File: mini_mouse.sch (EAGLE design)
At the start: 33 parts, among them IC1 PIC18F4550_TQFP, IC2 L298, IC3 LP2950CDT-5.0

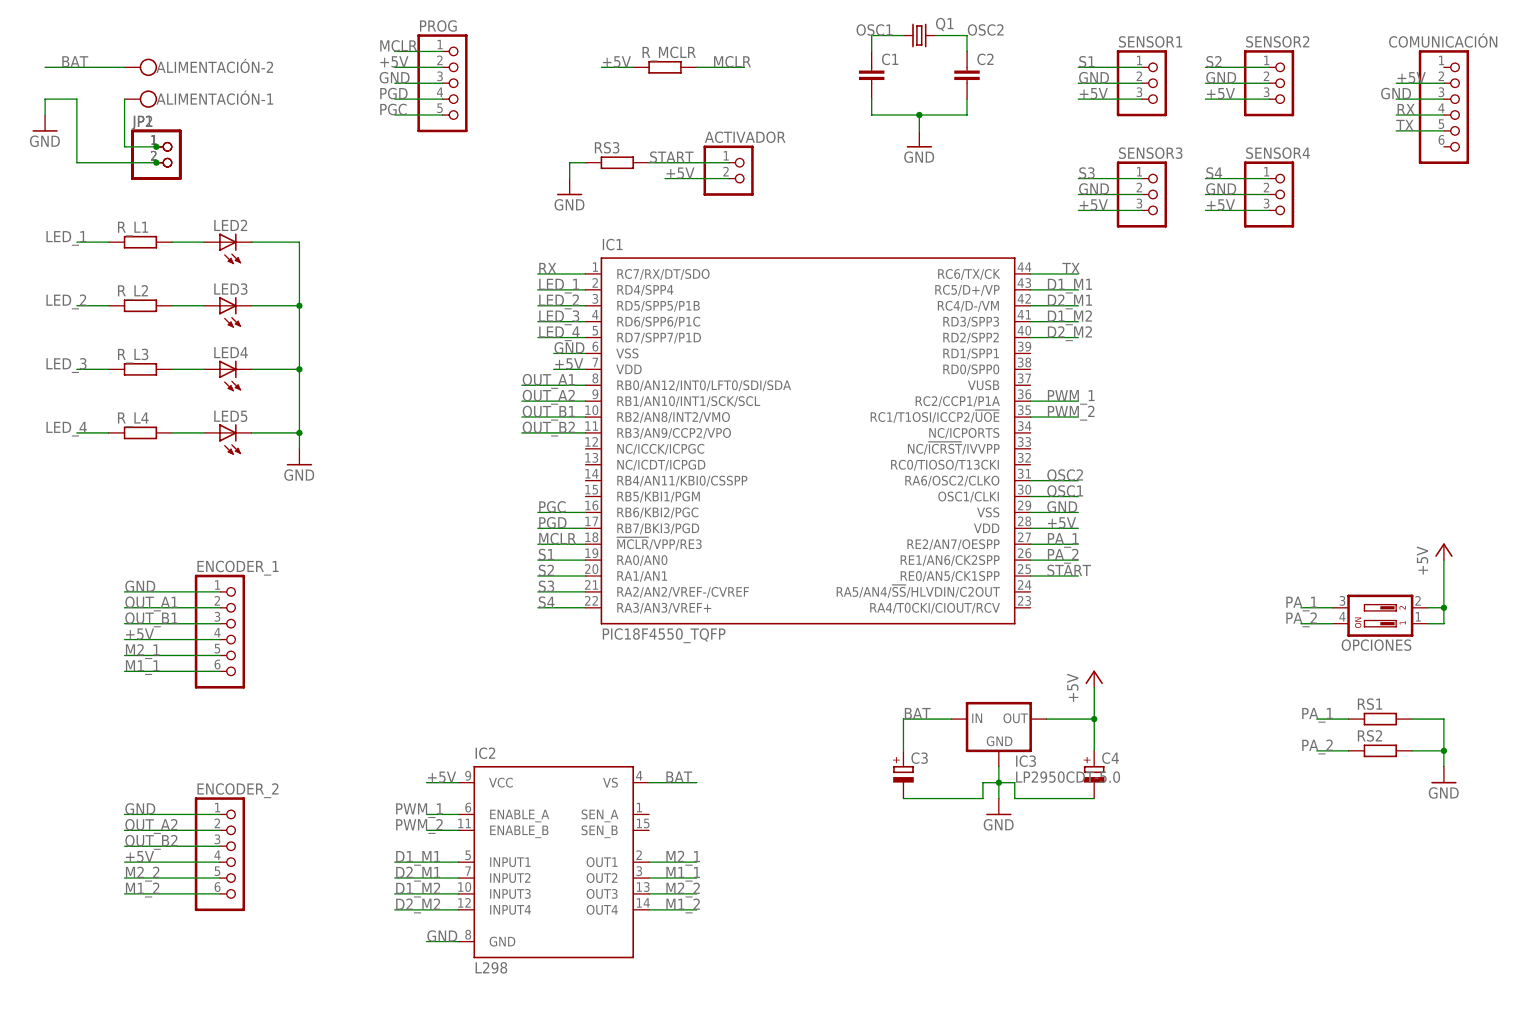
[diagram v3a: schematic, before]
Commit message: Cambios finales a esquemático, inicio de board
Se realizaron los ultimos cambios al esquemático. Se empezó el diseño del pcb
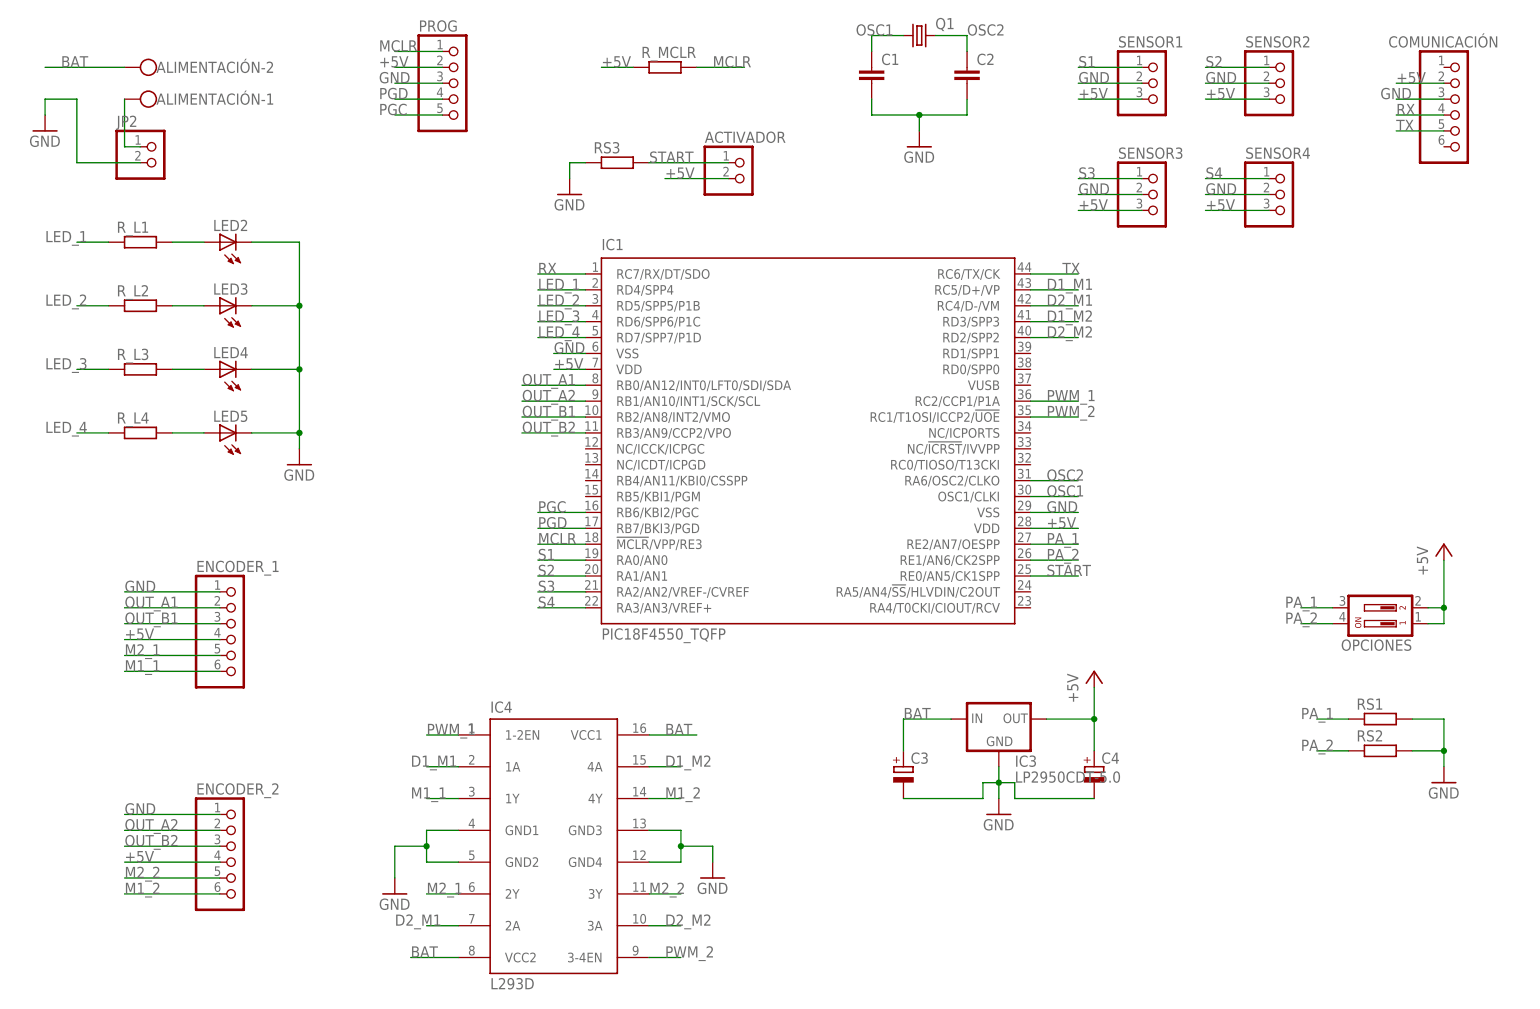
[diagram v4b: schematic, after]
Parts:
- removed IC2: L298, st-microelectronics:L298
- removed JP1: (no value), pinhead:PINHD-1X2
- added IC4: L293D, st-microelectronics:L293D
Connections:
- net +5V: no longer IC2.VCC
- net BAT: now also IC4.VCC1, IC4.VCC2; no longer IC2.VS
- net D1_M1: now also IC4.1A; no longer IC2.INPUT1
- net D1_M2: now also IC4.4A; no longer IC2.INPUT3
- net D2_M1: now also IC4.2A; no longer IC2.INPUT2
- net D2_M2: now also IC4.3A; no longer IC2.INPUT4
- net GND: now also IC4.GND1, IC4.GND2, IC4.GND3, IC4.GND4; no longer IC2.GND, JP1.2
- net M1_1: now also IC4.1Y; no longer IC2.OUT2
- net M1_2: now also IC4.4Y; no longer IC2.OUT4
- net M2_1: now also IC4.2Y; no longer IC2.OUT1
- net M2_2: now also IC4.3Y; no longer IC2.OUT3
- net N$5: no longer JP1.1
- net PWM_1: now also IC4.1-2EN; no longer IC2.ENABLE_A
- net PWM_2: now also IC4.3-4EN; no longer IC2.ENABLE_B
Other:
- moved on the sheet: JP2

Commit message: pcb
Se realizò PCB en un 90%
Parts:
- C3, C4: device rcl:CPOL-EU153CLV-0405 -> rcl:CPOL-EUE5-6
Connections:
- net D1_M1: now also IC1.RA4/T0CKI/CIOUT/RCV; no longer IC1.RC5/D+/VP
- net D1_M2: now also IC1.RB5/KBI1/PGM; no longer IC1.RD3/SPP3
- net D2_M1: now also IC1.RA5/AN4/!SS!/HLVDIN/C2OUT; no longer IC1.RC4/D-/VM
- net D2_M2: now also IC1.RB4/AN11/KBI0/CSSPP; no longer IC1.RD2/SPP2
- net LED_1: now also IC1.RC5/D+/VP
- net LED_2: now also IC1.RC4/D-/VM
- net LED_3: now also IC1.RD3/SPP3
- net LED_4: now also IC1.RD2/SPP2
- net M1_2: now also IC4.3Y; no longer IC4.4Y
- net M2_2: now also IC4.4Y; no longer IC4.3Y
- net OUT_B1: now also IC1.RB3/AN9/CCP2/VPO; no longer IC1.RB2/AN8/INT2/VMO
- net OUT_B2: now also IC1.RB2/AN8/INT2/VMO; no longer IC1.RB3/AN9/CCP2/VPO
- net PWM_1: now also IC1.RC1/T1OSI/ICCP2/!UOE; no longer IC1.RC2/CCP1/P1A
- net PWM_2: now also IC1.RC2/CCP1/P1A; no longer IC1.RC1/T1OSI/ICCP2/!UOE

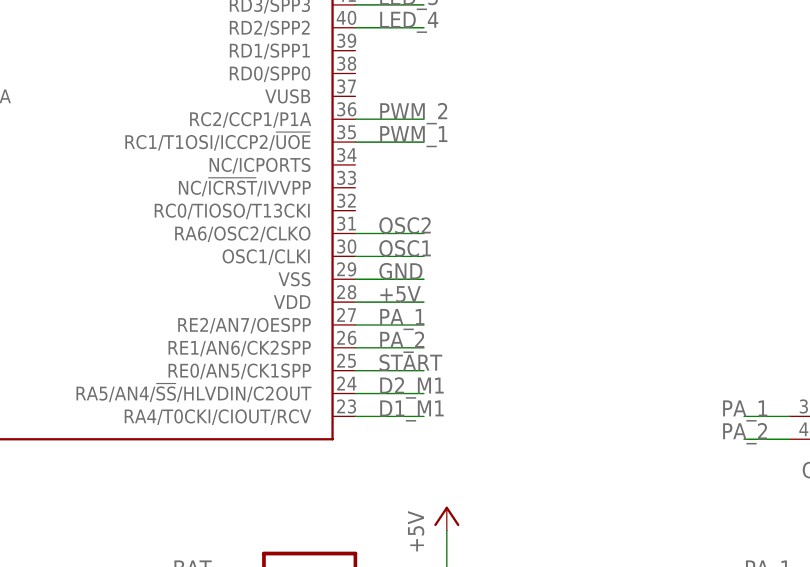
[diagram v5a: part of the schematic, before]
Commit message: Pads correctos
Se agregaron los pads deseados y se terminaron de cablear componentes faltantes
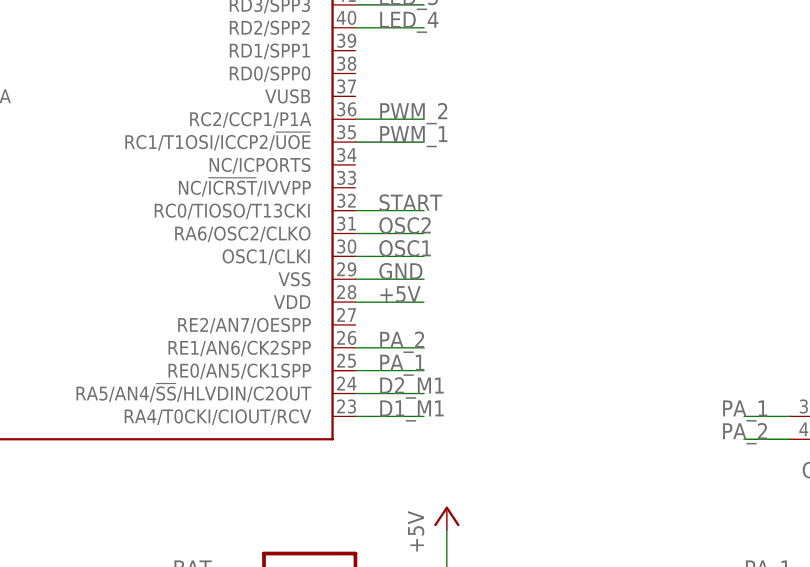
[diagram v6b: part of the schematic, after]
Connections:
- net PA_1: now also IC1.RE0/AN5/CK1SPP; no longer IC1.RE2/AN7/OESPP
- net START: now also IC1.RC0/TIOSO/T13CKI; no longer IC1.RE0/AN5/CK1SPP
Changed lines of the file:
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@@
 <net name="PA_1" class="0">
-<segment>
-<pinref part="IC1" gate="G$1" pin="RE2/AN7/OESPP"/>
-<wire x1="170.18" y1="83.82" x2="177.8" y2="83.82" width="0.1524" layer="91"/>
-<label x="172.72" y="83.82" size="1.778" layer="95"/>
-</segment>
 <segment>
 <pinref part="OPCIONES" gate="1" pin="3"/>
@@
 <label x="213.36" y="55.88" size="1.778" layer="95"/>
 </segment>
+<segment>
+<pinref part="IC1" gate="G$1" pin="RE0/AN5/CK1SPP"/>
+<wire x1="170.18" y1="78.74" x2="177.8" y2="78.74" width="0.1524" layer="91"/>
+<label x="172.72" y="78.74" size="1.778" layer="95"/>
+</segment>
 </net>
 <net name="PA_2" class="0">
-<segment>
-<pinref part="IC1" gate="G$1" pin="RE1/AN6/CK2SPP"/>
-<wire x1="170.18" y1="81.28" x2="177.8" y2="81.28" width="0.1524" layer="91"/>
-<label x="172.72" y="81.28" size="1.778" layer="95"/>
-</segment>
 <segment>
 <pinref part="OPCIONES" gate="1" pin="4"/>
@@
 <wire x1="220.98" y1="50.8" x2="215.9" y2="50.8" width="0.1524" layer="91"/>
 <label x="213.36" y="50.8" size="1.778" layer="95"/>
+</segment>
+<segment>
+<pinref part="IC1" gate="G$1" pin="RE1/AN6/CK2SPP"/>
+<wire x1="170.18" y1="81.28" x2="177.8" y2="81.28" width="0.1524" layer="91"/>
+<label x="172.72" y="81.28" size="1.778" layer="95"/>
 </segment>
 </net>
@@
 <net name="START" class="0">
 <segment>
-<pinref part="IC1" gate="G$1" pin="RE0/AN5/CK1SPP"/>
-<wire x1="170.18" y1="78.74" x2="177.8" y2="78.74" width="0.1524" layer="91"/>
-<label x="172.72" y="78.74" size="1.778" layer="95"/>
-</segment>
-<segment>
 <pinref part="ACTIVADOR" gate="G$1" pin="1"/>
 <wire x1="121.92" y1="144.78" x2="109.22" y2="144.78" width="0.1524" layer="91"/>
@@
 <pinref part="RS3" gate="G$1" pin="2"/>
 </segment>
+<segment>
+<pinref part="IC1" gate="G$1" pin="RC0/TIOSO/T13CKI"/>
+<wire x1="170.18" y1="96.52" x2="177.8" y2="96.52" width="0.1524" layer="91"/>
+<label x="172.72" y="96.52" size="1.778" layer="95"/>
+</segment>
 </net>
